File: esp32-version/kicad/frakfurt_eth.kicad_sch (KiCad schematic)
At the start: 42 parts, among them J1 HR911105A, J2 PROG, J4 Conn_Left_I2C, J5 Conn_01x02, U2 ESP32-WROOM-32, U3 LAN8720A, U4 SN65HVD232, U5 R-78B3.3-1.0 (Recom)

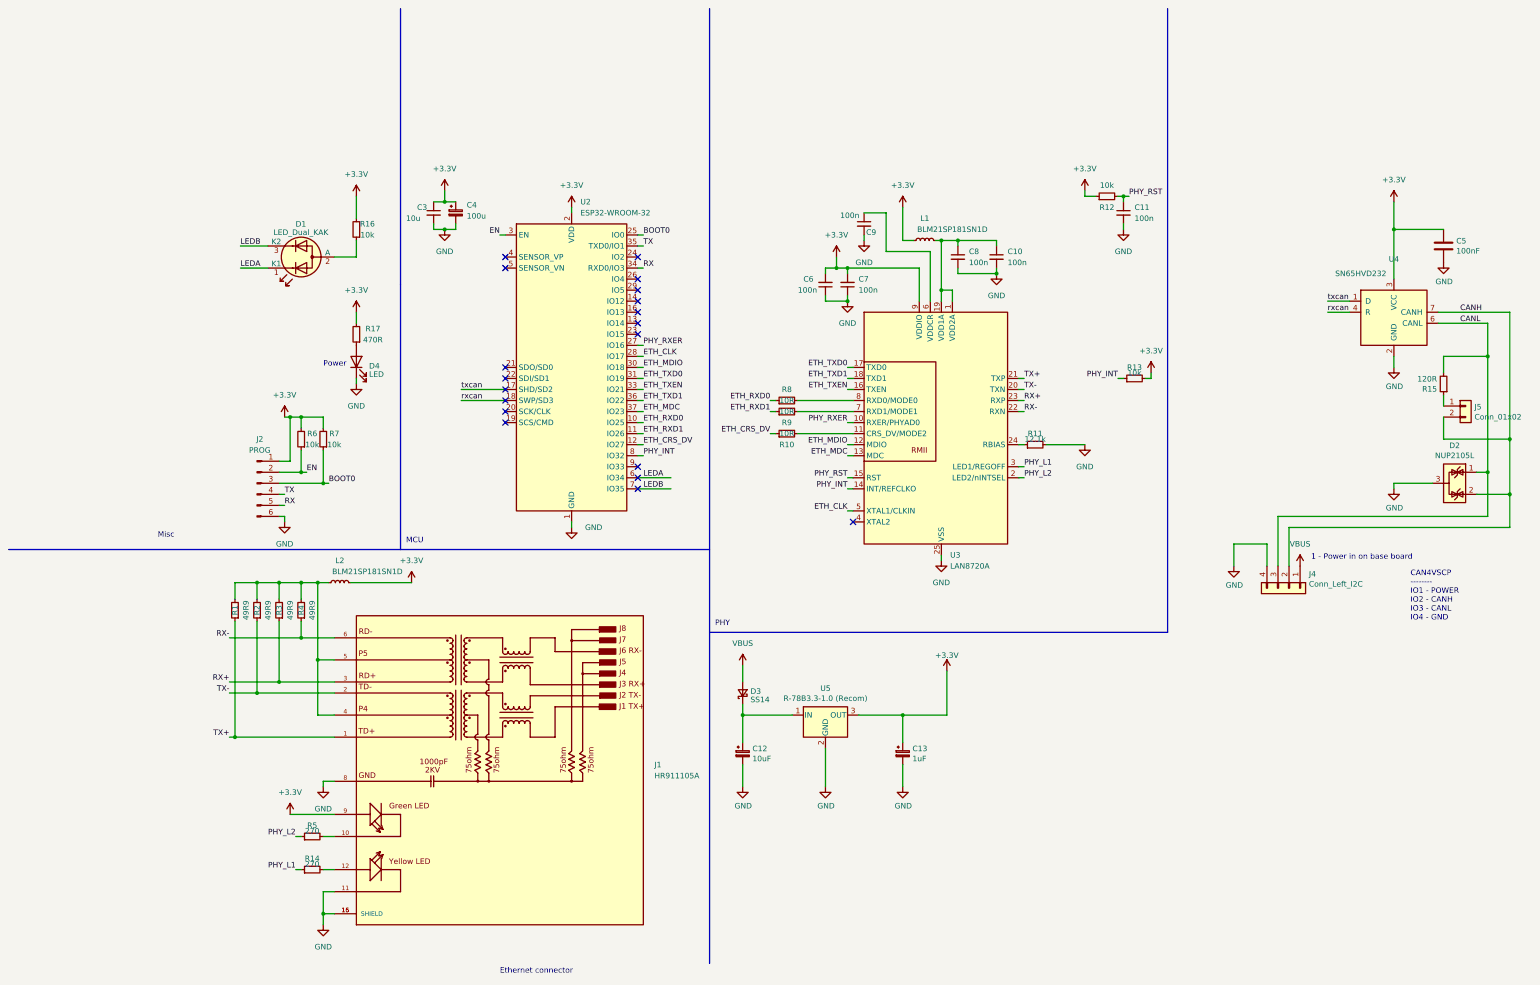
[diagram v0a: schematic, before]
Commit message: Translated schemas to KiCad format
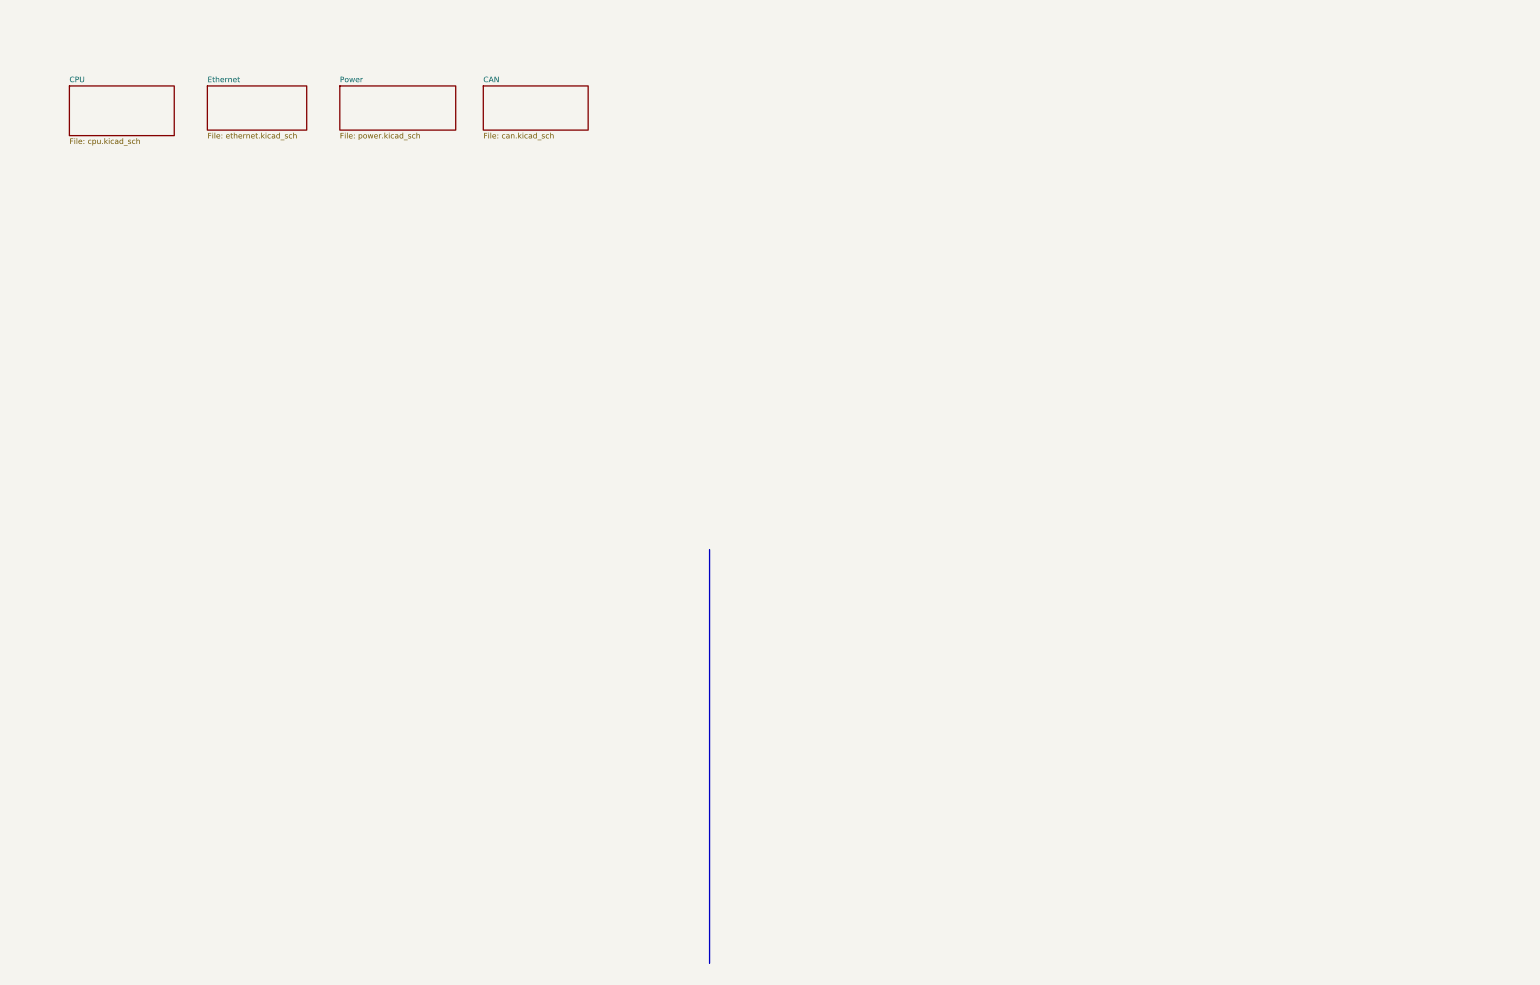
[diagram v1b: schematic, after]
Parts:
- removed C10, C11, C6, C7, C8, C9: 100n, Capacitor_SMD:C_0805_2012Metric_Pad1.18x1.45mm_HandSolder, symbol Device:C_Small
- removed C12: 10uF, Capacitor_SMD:C_0805_2012Metric_Pad1.18x1.45mm_HandSolder, symbol Device:CP_Small
- removed C13: 1uF, Capacitor_SMD:C_0805_2012Metric_Pad1.18x1.45mm_HandSolder, symbol Device:CP_Small
- removed C3: 10u, Capacitor_SMD:C_0805_2012Metric_Pad1.18x1.45mm_HandSolder, symbol Device:C_Small
- removed C4: 100u, Capacitor_Tantalum_SMD:CP_EIA-3528-21_Kemet-B, symbol Device:C_Polarized_Small
- removed C5: 100nF, Capacitor_SMD:C_0805_2012Metric, symbol Device:C
- removed D1: LED_Dual_KAK, LED_THT:LED_D5.0mm-3, symbol Device:LED_Dual_KAK
- removed D2: NUP2105L, Package_TO_SOT_SMD:SOT-23, symbol Power_Protection:NUP2105L
- removed D3: SS14, Diode_SMD:D_SMA, symbol Device:D_Schottky_Small
- removed D4: LED, LED_SMD:LED_0805_2012Metric_Pad1.15x1.40mm_HandSolder, symbol Device:LED
- removed J1: HR911105A, lib:HANRUN_HR911105A, symbol HR911105A:HR911105A
- removed J2: PROG, Connector_PinHeader_2.54mm:PinHeader_1x06_P2.54mm_Vertical, symbol Connector:Conn_01x06_Male
- removed J4: Conn_Left_I2C, Connector_PinHeader_2.54mm:PinHeader_1x04_P2.54mm_Vertical, symbol Connector_Generic:Conn_01x04
- removed J5: Conn_01x02, Connector_PinHeader_2.54mm:PinHeader_1x02_P2.54mm_Vertical, symbol Connector_Generic:Conn_01x02
- removed L1, L2: BLM21SP181SN1D, Resistor_SMD:R_0805_2012Metric_Pad1.20x1.40mm_HandSolder, symbol Device:L_Small
- removed R1, R2, R3, R4: 49R9, Resistor_SMD:R_0805_2012Metric_Pad1.20x1.40mm_HandSolder, symbol Device:R_Small
- removed R10, R8, R9: 10R, Resistor_SMD:R_0805_2012Metric_Pad1.20x1.40mm_HandSolder, symbol Device:R_Small
- removed R11: 12.1k, Resistor_SMD:R_0805_2012Metric_Pad1.20x1.40mm_HandSolder, symbol Device:R_Small
- removed R12, R13, R16, R6, R7: 10k, Resistor_SMD:R_0805_2012Metric_Pad1.20x1.40mm_HandSolder, symbol Device:R_Small
- removed R14, R5: 270, Resistor_SMD:R_0805_2012Metric_Pad1.20x1.40mm_HandSolder, symbol Device:R_Small
- removed R15: 120R, Resistor_SMD:R_0805_2012Metric, symbol Device:R_Small
- removed R17: 470R, Resistor_SMD:R_0805_2012Metric_Pad1.20x1.40mm_HandSolder, symbol Device:R_Small
- removed U2: ESP32-WROOM-32, RF_Module:ESP32-WROOM-32, symbol RF_Module:ESP32-WROOM-32
- removed U3: LAN8720A, Package_DFN_QFN:QFN-24-1EP_4x4mm_P0.5mm_EP2.6x2.6mm, symbol Interface_Ethernet:LAN8720A
- removed U4: SN65HVD232, Package_SO:SOIC-8_3.9x4.9mm_P1.27mm, symbol Interface_CAN_LIN:SN65HVD232
- removed U5: R-78B3.3-1.0 (Recom), Converter_DCDC:Converter_DCDC_RECOM_R-78B-2.0_THT, symbol Regulator_Switching:R-78B3.3-2.0
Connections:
- no-connect marks 19 -> 0
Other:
- added sheet CAN (can.kicad_sch)
- added sheet CPU (cpu.kicad_sch)
- added sheet Ethernet (ethernet.kicad_sch)
- added sheet Power (power.kicad_sch)
- note removed: "1 - Power in on base board"
- note removed: "CAN4VSCP -------- IO1 - POWER IO2 - CANH IO3 - CANL IO4 - GND"
- note removed: "Ethernet connector"
- note removed: "MCU"
- note removed: "Misc"
- note removed: "PHY"
- note removed: "Power"
